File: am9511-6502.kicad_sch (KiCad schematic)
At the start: 14 parts, among them J1 Conn_01x18_Pin, U1 AM9511A, U2 ATF16V8B, U3 74HC112, U4 ADA-TPS61040, U5 74HC123, X1 4 MHz

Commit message: additional PCB cleanup
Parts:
- D1, D2: footprint LED_THT:LED_D5.0mm -> LED_THT:LED_D3.0mm
- J1: footprint Connector_PinHeader_2.54mm:PinHeader_1x18_P2.54mm_Horizontal -> am9511-6502-footprints:PinHeader_1x18_P2.54mm_Horizontal
- U4: footprint Local:ADA-TPS61040 -> am9511-6502-footprints:ADA-TPS61040
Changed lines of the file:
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@@
 			)
 		)
-		(property "Footprint" "Local:ADA-TPS61040"
+		(property "Footprint" "am9511-6502-footprints:ADA-TPS61040"
 			(at 164.592 66.802 0)
 			(effects
@@
 			)
 		)
-		(property "Footprint" "Connector_PinHeader_2.54mm:PinHeader_1x18_P2.54mm_Horizontal"
+		(property "Footprint" "am9511-6502-footprints:PinHeader_1x18_P2.54mm_Horizontal"
 			(at 34.29 60.96 0)
 			(effects
@@
 			)
 		)
-		(property "Footprint" "LED_THT:LED_D5.0mm"
+		(property "Footprint" "LED_THT:LED_D3.0mm"
 			(at 224.79 69.85 0)
 			(effects
@@
 			)
 		)
-		(property "Footprint" "LED_THT:LED_D5.0mm"
+		(property "Footprint" "LED_THT:LED_D3.0mm"
 			(at 204.47 69.85 0)
 			(effects

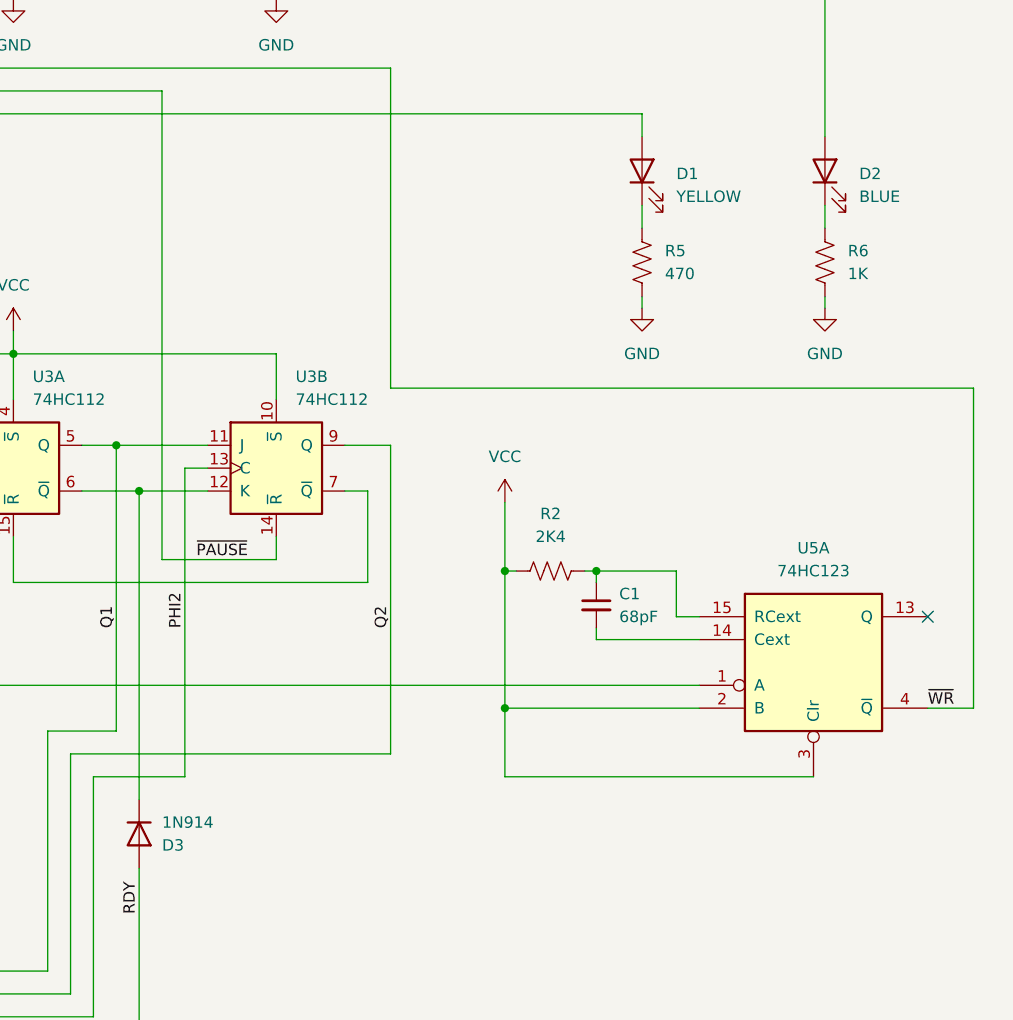
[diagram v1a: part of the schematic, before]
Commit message: reset schematic annotations
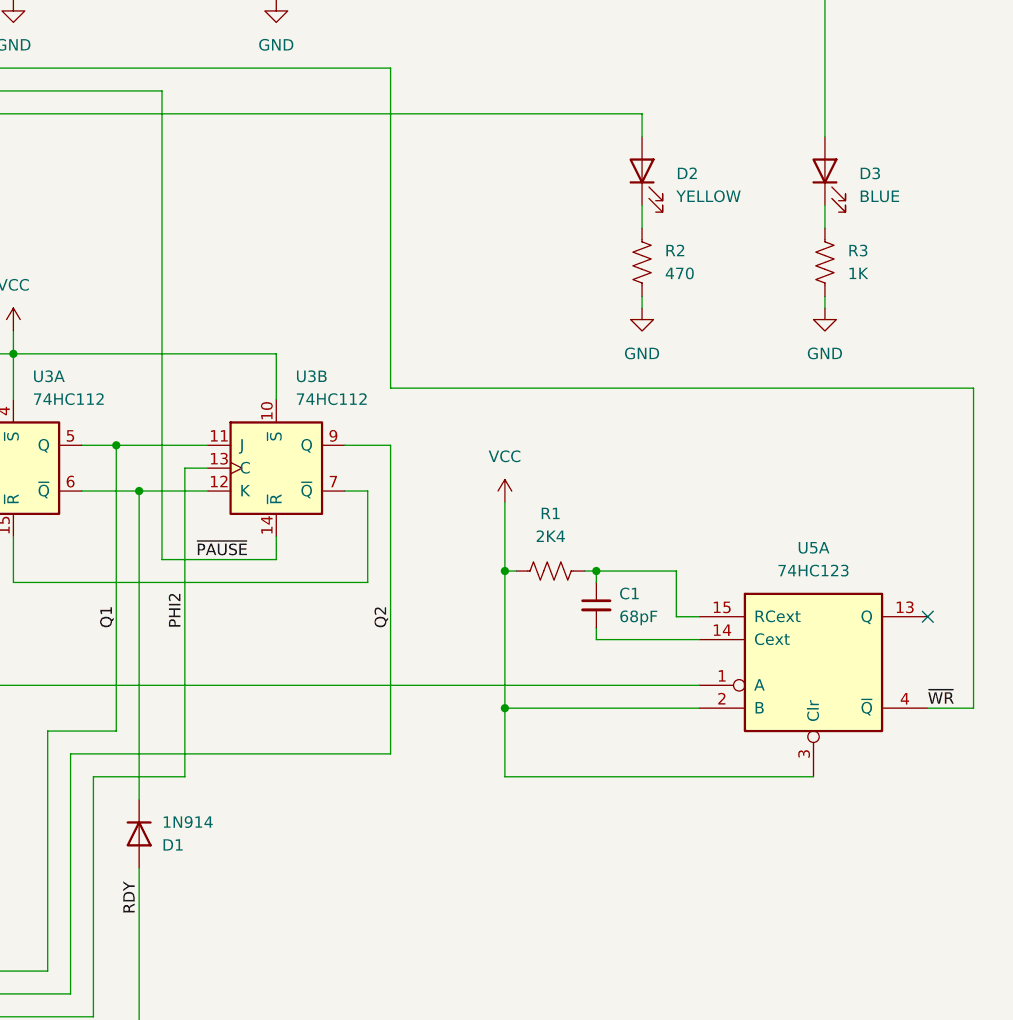
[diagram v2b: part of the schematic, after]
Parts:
- renumbered D3 to D1, D1 to D2, D2 to D3, R2 to R1, R5 to R2, R6 to R3
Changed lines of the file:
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@@
 		(dnp no)
 		(fields_autoplaced yes)
-		(property "Reference" "R5"
+		(property "Reference" "R2"
 			(at 207.01 78.7399 0)
 			(effects
@@
 			(project ""
 				(path "/492d2c5d-68ab-43c4-8db3-0d52dc374f84"
-					(reference "R5")
+					(reference "R2")
 					(unit 1)
 				)
@@
 		(dnp no)
 		(fields_autoplaced yes)
-		(property "Reference" "R2"
+		(property "Reference" "R1"
 			(at 194.31 107.95 90)
 			(effects
@@
 			(project "am9511-6502"
 				(path "/492d2c5d-68ab-43c4-8db3-0d52dc374f84"
-					(reference "R2")
+					(reference "R1")
 					(unit 1)
 				)
@@
 		(dnp no)
 		(fields_autoplaced yes)
-		(property "Reference" "#PWR025"
+		(property "Reference" "#PWR014"
 			(at 204.47 91.44 0)
 			(effects
@@
 			(project ""
 				(path "/492d2c5d-68ab-43c4-8db3-0d52dc374f84"
-					(reference "#PWR025")
+					(reference "#PWR014")
 					(unit 1)
 				)
@@
 		(dnp no)
 		(fields_autoplaced yes)
-		(property "Reference" "R6"
+		(property "Reference" "R3"
 			(at 227.33 78.7399 0)
 			(effects
@@
 			(project "am9511-6502"
 				(path "/492d2c5d-68ab-43c4-8db3-0d52dc374f84"
-					(reference "R6")
+					(reference "R3")
 					(unit 1)
 				)
@@
 		(dnp no)
 		(fields_autoplaced yes)
-		(property "Reference" "#PWR024"
+		(property "Reference" "#PWR015"
 			(at 224.79 49.53 0)
 			(effects
@@
 			(project ""
 				(path "/492d2c5d-68ab-43c4-8db3-0d52dc374f84"
-					(reference "#PWR024")
+					(reference "#PWR015")
 					(unit 1)
 				)
@@
 		(on_board yes)
 		(dnp no)
-		(property "Reference" "D3"
+		(property "Reference" "D1"
 			(at 151.13 144.7801 90)
 			(effects
@@
 			(project "am9511-6502"
 				(path "/492d2c5d-68ab-43c4-8db3-0d52dc374f84"
-					(reference "D3")
+					(reference "D1")
 					(unit 1)
 				)
@@
 		(dnp no)
 		(fields_autoplaced yes)
-		(property "Reference" "#PWR027"
+		(property "Reference" "#PWR016"
 			(at 224.79 91.44 0)
 			(effects
@@
 			(project "am9511-6502"
 				(path "/492d2c5d-68ab-43c4-8db3-0d52dc374f84"
-					(reference "#PWR027")
+					(reference "#PWR016")
 					(unit 1)
 				)
@@
 		(dnp no)
 		(fields_autoplaced yes)
-		(property "Reference" "D2"
+		(property "Reference" "D3"
 			(at 228.6 70.1674 90)
 			(effects
@@
 			(project "am9511-6502"
 				(path "/492d2c5d-68ab-43c4-8db3-0d52dc374f84"
-					(reference "D2")
+					(reference "D3")
 					(unit 1)
 				)
@@
 		(dnp no)
 		(fields_autoplaced yes)
-		(property "Reference" "D1"
+		(property "Reference" "D2"
 			(at 208.28 70.1674 90)
 			(effects
@@
 			(project ""
 				(path "/492d2c5d-68ab-43c4-8db3-0d52dc374f84"
-					(reference "D1")
-					(unit 1)
-				)
+					(reference "D2")
+					(unit 1)
+				)
